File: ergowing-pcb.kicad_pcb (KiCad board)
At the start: 2 copper layers, 156 parts, among them J1 USB_mini_micro_B, K0:0 KEYSW, K0:1 KEYSW, K0:2 KEYSW, K0:3 KEYSW, K0:4 KEYSW, K10:0 KEYSW, K10:1 KEYSW, K10:2 KEYSW, K10:3 KEYSW, K10:4 KEYSW, K11:0 KEYSW, K11:1 KEYSW, K11:2 KEYSW, K11:3 KEYSW, K11:4 KEYSW, K12:0 KEYSW, K12:1 KEYSW, K12:2 KEYSW, K12:3 KEYSW, K12:4 KEYSW, K13:0 KEYSW, K13:1 KEYSW, K13:2 KEYSW, K13:3 KEYSW, K13:4 KEYSW, K1:0 KEYSW, K1:1 KEYSW, K1:2 KEYSW, K1:3 KEYSW, K1:4 KEYSW, K2:0 KEYSW, K2:1 KEYSW, K2:2 KEYSW, K2:3 KEYSW, K2:4 KEYSW, K3:0 KEYSW, K3:1 KEYSW, K3:2 KEYSW, K3:3 KEYSW, K3:4 KEYSW, K4:0 KEYSW, K4:1 KEYSW, K4:2 KEYSW, K4:3 KEYSW, K4:4 KEYSW, K5:0 KEYSW, K5:1 KEYSW, K5:2 KEYSW, K5:3 KEYSW, K5:4 KEYSW, K6:0 KEYSW, K6:1 KEYSW, K6:3 KEYSW, K7:0 KEYSW, K7:1 KEYSW, K7:3 KEYSW, K7:4 KEYSW, K8:0 KEYSW, K8:1 KEYSW, K8:2 KEYSW, K8:3 KEYSW, K8:4 KEYSW, K9:0 KEYSW, K9:1 KEYSW, K9:2 KEYSW, K9:3 KEYSW, K9:4 KEYSW, SW1 SW_PUSH, U1 ATMEGA32U4, X1 XTAL_GND

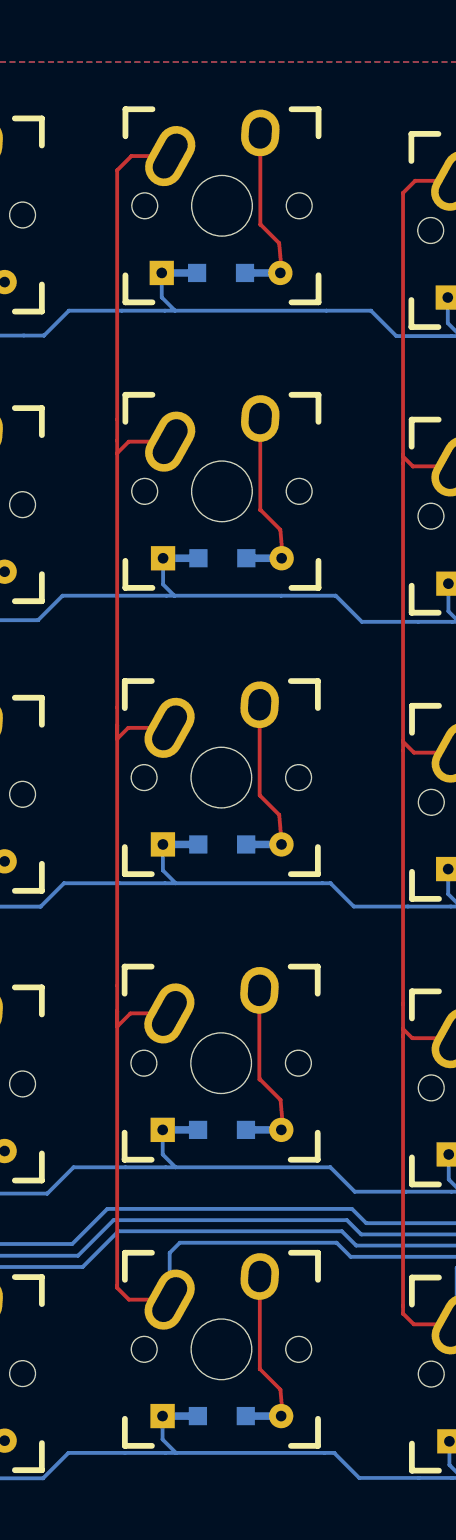
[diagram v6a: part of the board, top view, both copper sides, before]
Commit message: Col3 re-aligned
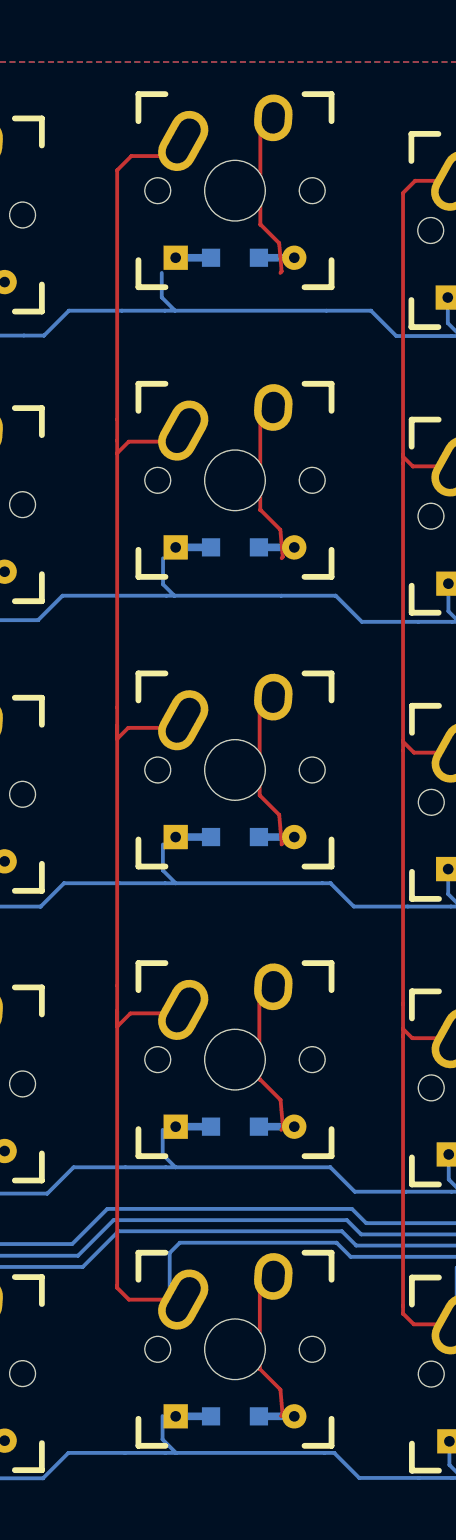
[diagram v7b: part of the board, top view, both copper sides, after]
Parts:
- moved D3:0 1.36 mm to (126.5, 164.7)
- moved K3:0 1.31 mm to (126.5, 160.2)
- moved K3:1 1.12 mm to (126.5, 179.3)
- moved D3:1 1.10 mm to (126.5, 183.7)
- moved K3:2 1.03 mm to (126.5, 198.3)
- moved D3:2 0.97 mm to (126.5, 202.8)
- moved K3:3 0.94 mm to (126.5, 217.4)
- moved K3:4 0.89 mm to (126.5, 236.4)
- moved D3:3 0.88 mm to (126.5, 221.8)
- moved D3:4 0.86 mm to (126.5, 240.9)
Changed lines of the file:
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@@
   )
   (module keyboard_parts:D_SOD123_axial (layer B.Cu)
-    (at 125.612235 165.65705)
+    (at 126.528438 164.656682)
     (attr smd)
     (fp_text reference D3:0 (at 0 -1.925) (layer B.SilkS)
@@
   )
   (module keyboard_parts:D_SOD123_axial (layer B.Cu)
-    (at 125.69795 184.420986)
+    (at 126.528438 183.706682)
     (attr smd)
     (fp_text reference D3:1 (at 0 -1.925) (layer B.SilkS)
@@
   )
   (module keyboard_parts:D_SOD123_axial (layer B.Cu)
-    (at 125.688399 203.243449)
+    (at 126.528438 202.756682)
     (attr smd)
     (fp_text reference D3:2 (at 0 -1.925) (layer B.SilkS)
@@
   )
   (module keyboard_parts:D_SOD123_axial (layer B.Cu)
-    (at 125.674489 222.016096)
+    (at 126.528438 221.806682)
     (attr smd)
     (fp_text reference D3:3 (at 0 -1.925) (layer B.SilkS)
@@
   )
   (module keyboard_parts:D_SOD123_axial (layer B.Cu)
-    (at 125.664933 240.838549)
+    (at 126.528438 240.856682)
     (attr smd)
     (fp_text reference D3:4 (at 0 -1.925) (layer B.SilkS)
@@
   )
   (module keebs:Mx_Alps_100_R-5deg (layer F.Cu)
-    (at 125.673721 161.239691 5)
+    (at 126.528438 160.245778 5)
     (descr MXALPS)
     (tags MXALPS)
@@
   )
   (module keebs:Mx_Alps_100_R-5deg (layer F.Cu)
-    (at 125.670644 180.021422 5)
+    (at 126.528438 179.295778 5)
     (descr MXALPS)
     (tags MXALPS)
@@
   )
   (module keebs:Mx_Alps_100_R-5deg (layer F.Cu)
-    (at 125.631205 198.846494 5)
+    (at 126.528438 198.345778 5)
     (descr MXALPS)
     (tags MXALPS)
@@
   )
   (module keebs:Mx_Alps_100_R-5deg (layer F.Cu)
-    (at 125.618167 217.629107 5)
+    (at 126.528438 217.395778 5)
     (descr MXALPS)
     (tags MXALPS)
@@
   )
   (module keebs:Mx_Alps_100_R-5deg (layer F.Cu)
-    (at 125.638503 236.448949 5)
+    (at 126.528438 236.445778 5)
     (descr MXALPS)
     (tags MXALPS)

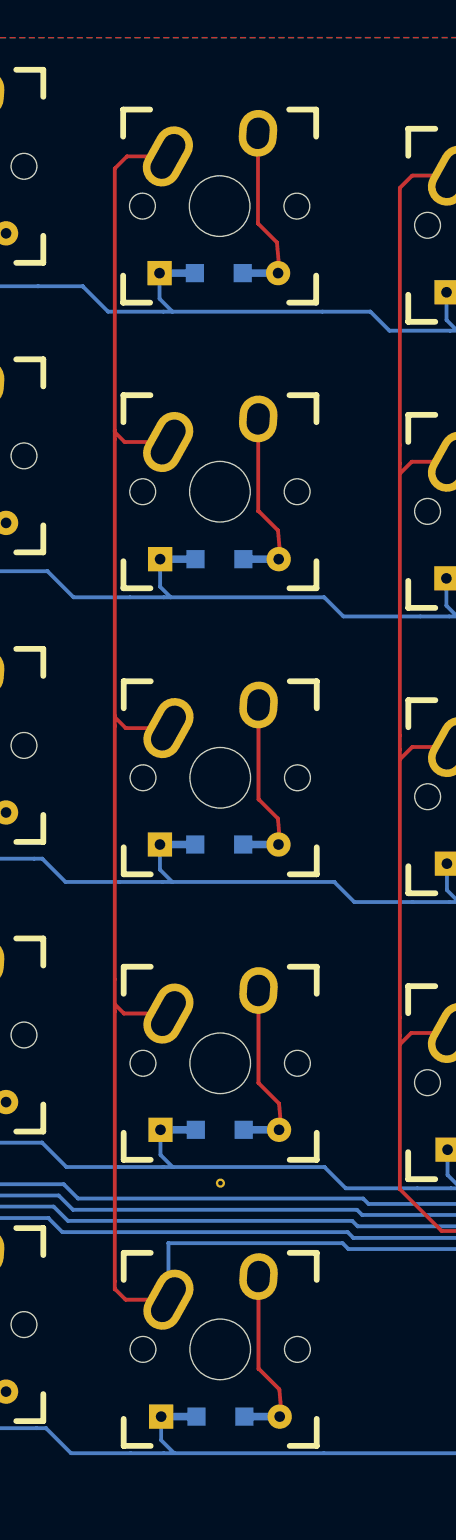
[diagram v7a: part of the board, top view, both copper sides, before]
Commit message: Col4 re-aligned
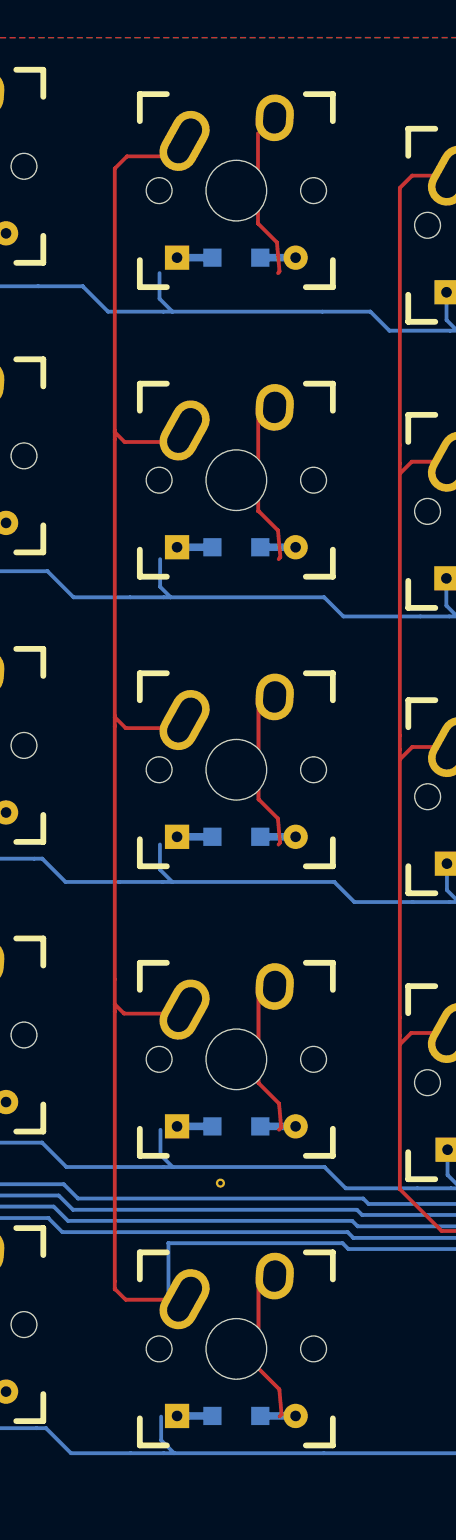
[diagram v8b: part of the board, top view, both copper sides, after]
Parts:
- moved D4:0 1.54 mm to (145.6, 166.3)
- moved K4:0 1.50 mm to (145.6, 161.8)
- moved D4:1 1.36 mm to (145.6, 185.3)
- moved K4:1 1.32 mm to (145.6, 180.9)
- moved D4:2 1.24 mm to (145.6, 204.4)
- moved K4:2 1.18 mm to (145.6, 199.9)
- moved D4:3 1.11 mm to (145.6, 223.4)
- moved K4:3 1.09 mm to (145.6, 219.0)
- moved K4:4 1.06 mm to (145.6, 238.0)
- moved D4:4 1.05 mm to (145.6, 242.5)
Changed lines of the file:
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@@
   )
   (module keyboard_parts:D_SOD123_axial (layer B.Cu)
-    (at 144.424712 167.27359)
+    (at 145.578438 166.256682)
     (attr smd)
     (fp_text reference D4:0 (at 0 -1.925) (layer B.SilkS)
@@
   )
   (module keyboard_parts:D_SOD123_axial (layer B.Cu)
-    (at 144.464971 186.091689)
+    (at 145.578438 185.306682)
     (attr smd)
     (fp_text reference D4:1 (at 0 -1.925) (layer B.SilkS)
@@
   )
   (module keyboard_parts:D_SOD123_axial (layer B.Cu)
-    (at 144.451063 204.86434)
+    (at 145.578438 204.356682)
     (attr smd)
     (fp_text reference D4:2 (at 0 -1.925) (layer B.SilkS)
@@
   )
   (module keyboard_parts:D_SOD123_axial (layer B.Cu)
-    (at 144.486963 223.632635)
+    (at 145.578438 223.406682)
     (attr smd)
     (fp_text reference D4:3 (at 0 -1.925) (layer B.SilkS)
@@
   )
   (module keyboard_parts:D_SOD123_axial (layer B.Cu)
-    (at 144.531579 242.500535)
+    (at 145.578438 242.456682)
     (attr smd)
     (fp_text reference D4:4 (at 0 -1.925) (layer B.SilkS)
@@
   )
   (module keebs:Mx_Alps_100_R-5deg (layer F.Cu)
-    (at 144.480645 162.864433 5)
+    (at 145.578438 161.845778 5)
     (descr MXALPS)
     (tags MXALPS)
@@
   )
   (module keebs:Mx_Alps_100_R-5deg (layer F.Cu)
-    (at 144.498363 181.654394 5)
+    (at 145.578438 180.895778 5)
     (descr MXALPS)
     (tags MXALPS)
@@
   )
   (module keebs:Mx_Alps_100_R-5deg (layer F.Cu)
-    (at 144.518693 200.474239 5)
+    (at 145.578438 199.945778 5)
     (descr MXALPS)
     (tags MXALPS)
@@
   )
   (module keebs:Mx_Alps_100_R-5deg (layer F.Cu)
-    (at 144.515626 219.255975 5)
+    (at 145.578438 218.995778 5)
     (descr MXALPS)
     (tags MXALPS)
@@
   )
   (module keebs:Mx_Alps_100_R-5deg (layer F.Cu)
-    (at 144.516034 238.077564 5)
+    (at 145.578438 238.045778 5)
     (descr MXALPS)
     (tags MXALPS)
